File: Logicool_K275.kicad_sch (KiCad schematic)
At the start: 33 parts, among them IC1 RP2040_QFN56, J1 Conn_01x05, J2 Conn_01x24, SW3 SW_Push, SW4 SW_Push, U3 24LC1025, U4 AP2112K-3.3, U5 W25Q32JVSS, Y1 Crystal

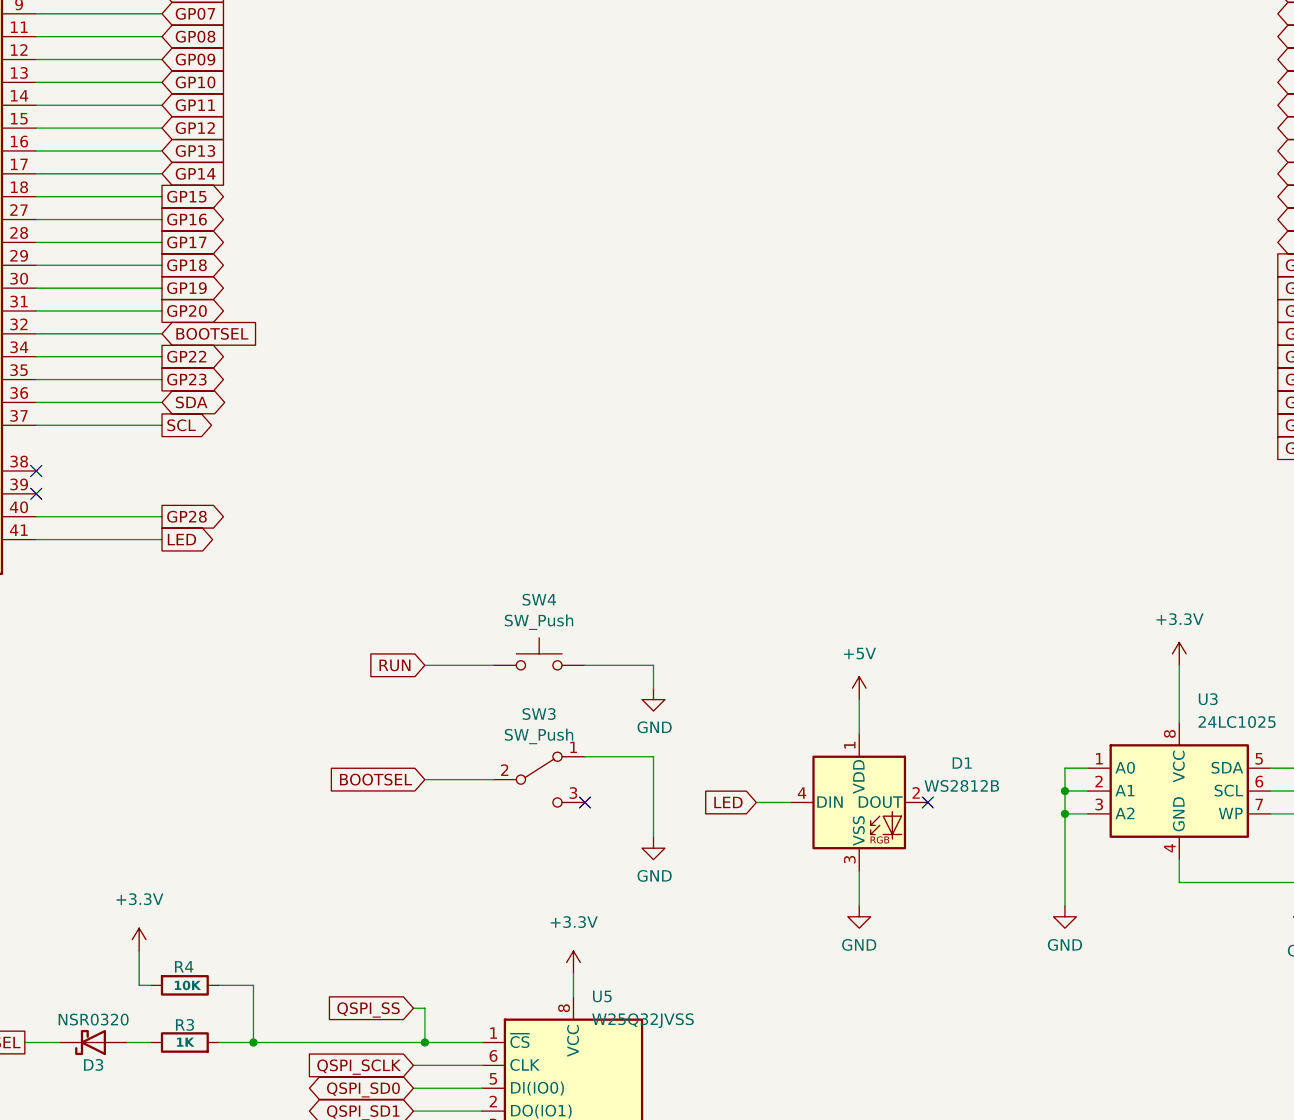
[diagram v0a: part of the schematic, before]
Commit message: Neopixelの信号線にレベル変換を追加
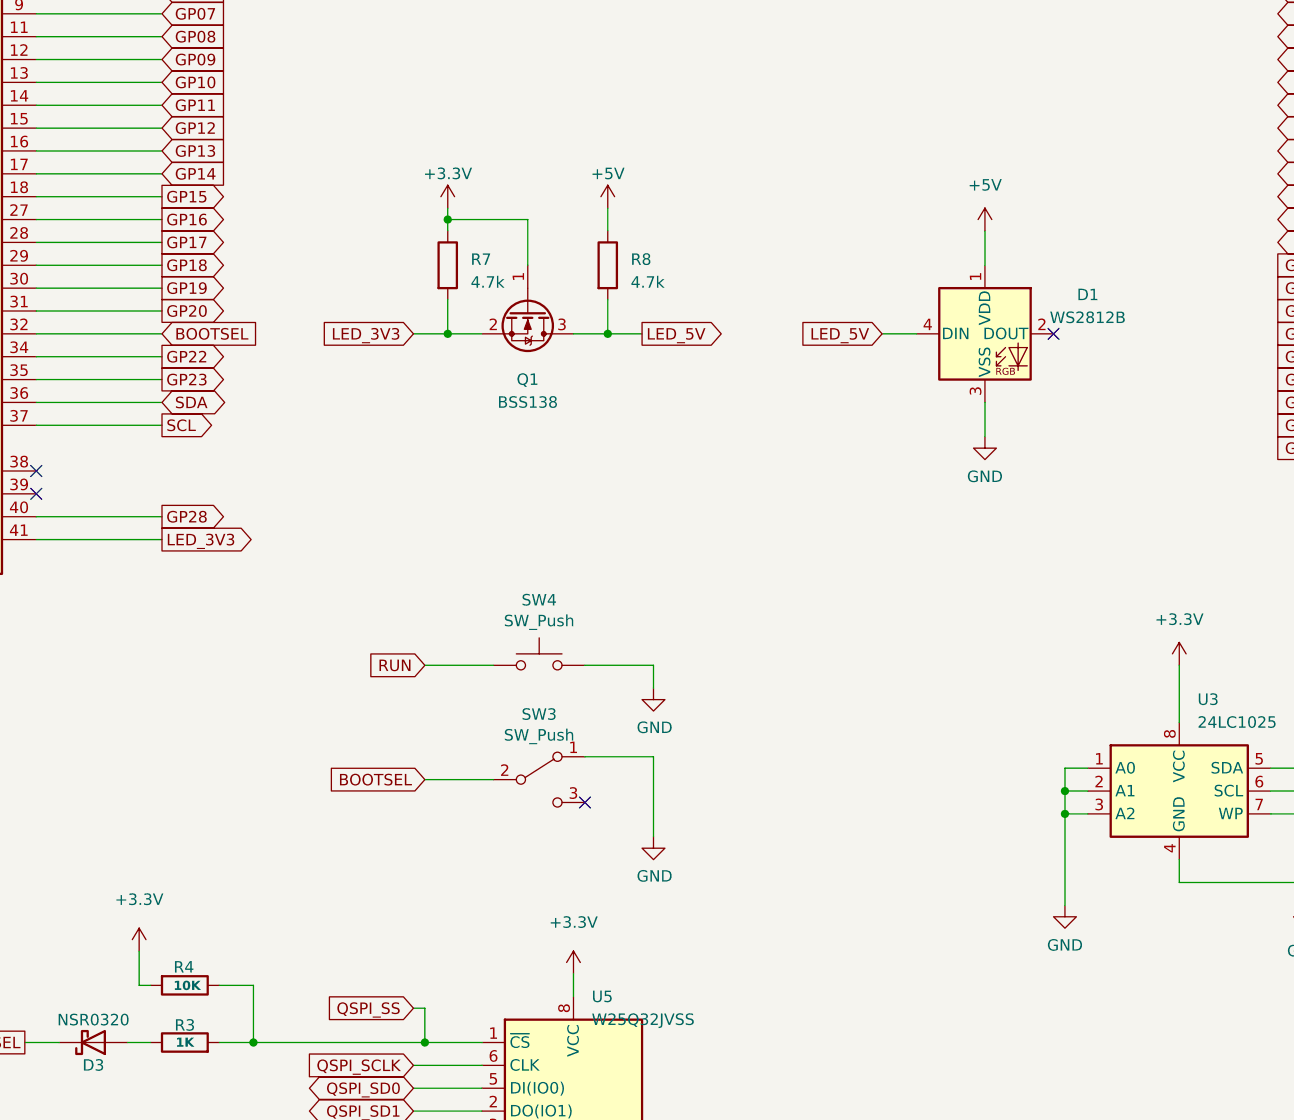
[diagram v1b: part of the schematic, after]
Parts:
- added Q1: BSS138, Package_TO_SOT_SMD:SOT-23, symbol Transistor_FET:BSS138
- added R7, R8: 4.7k, Resistor_SMD:R_0603_1608Metric_Pad0.98x0.95mm_HandSolder, symbol Device:R
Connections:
- net +3.3V: now also Q1.1 (G), R7.1
- net +5V: now also R8.1
- net LED renamed LED_3V3
- net LED_3V3: now also Q1.2 (S), R7.2; no longer D1.4 (DIN)
- new net LED_5V: D1.4 (DIN), Q1.3 (D), R8.2
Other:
- moved on the sheet: D1
